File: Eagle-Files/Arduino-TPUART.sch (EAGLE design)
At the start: 18 parts, among them Q1 4,915MHz

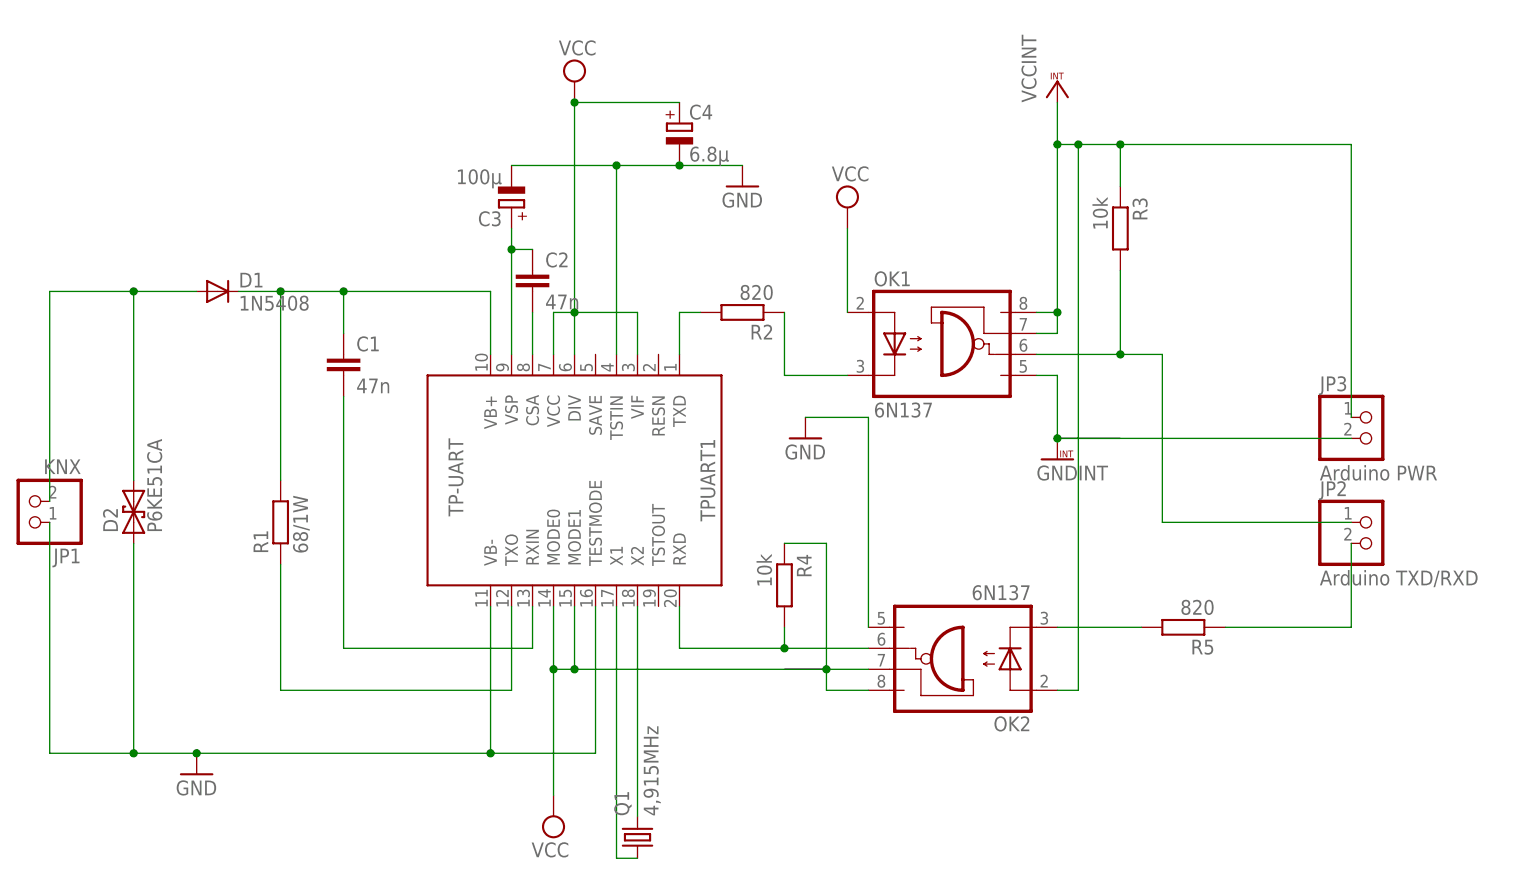
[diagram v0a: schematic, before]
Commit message: Update schematic with actually used parts and their correct packages.
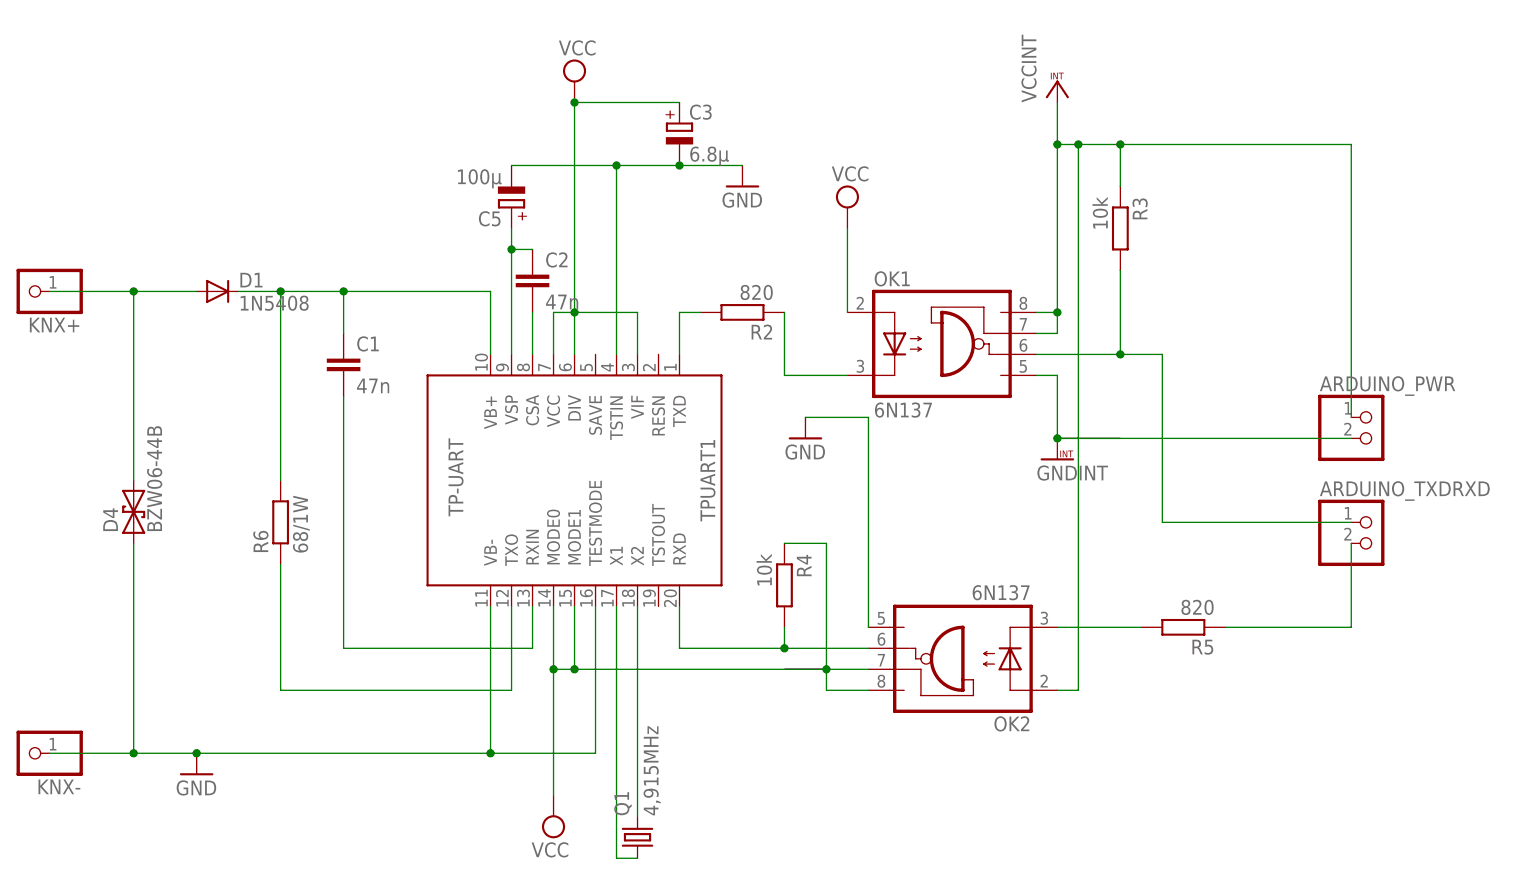
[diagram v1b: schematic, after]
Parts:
- removed C4: 6.8µ, rcl:CPOL-EUE5-4
- removed D2: P6KE51CA, diode:15KEXXC
- removed JP1: KNX, pinhead:PINHD-1X2
- removed R1: 68/1W, resistor:R-EU_0207/10
- added C5: 100µ, resistor:CPOL-EUE2.5-5
- added D4: BZW06-44B, diode:BZW04XXB
- added KNX+, KNX-: (no value), pinhead:PINHD-1X1
- added R6: 68/1W, resistor:R-EU_0414/15
- ARDUINO_PWR: value Arduino PWR -> (none)
- ARDUINO_TXDRXD: value Arduino TXD/RXD -> (none)
- C3: value 100µ -> 6.8µ; device rcl:CPOL-EUE5-4 -> resistor:CPOL-EUE2-5
- R2, R3, R4, R5: device resistor:R-EU_0207/10 -> resistor:R-EU_0411/12
- renumbered JP2 to ARDUINO_TXDRXD, JP3 to ARDUINO_PWR
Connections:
- net N$11 renamed ARDUINO_RXD
- net N$13 renamed ARDUINO_TXD
- removed net N$2: D1.A, D2.2, JP1.2
- new net KNX+: D1.A, D4.2, KNX+.1
- net GND: now also C5.-, D4.1, KNX-.1; no longer C4.-, D2.1, JP1.1
- net N$1: now also R6.2; no longer R1.2
- net N$3: now also R6.1; no longer R1.1
- net N$6: now also C5.+; no longer C3.+
- net VCC: now also C3.+; no longer C4.+
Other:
- moved on the sheet: C3

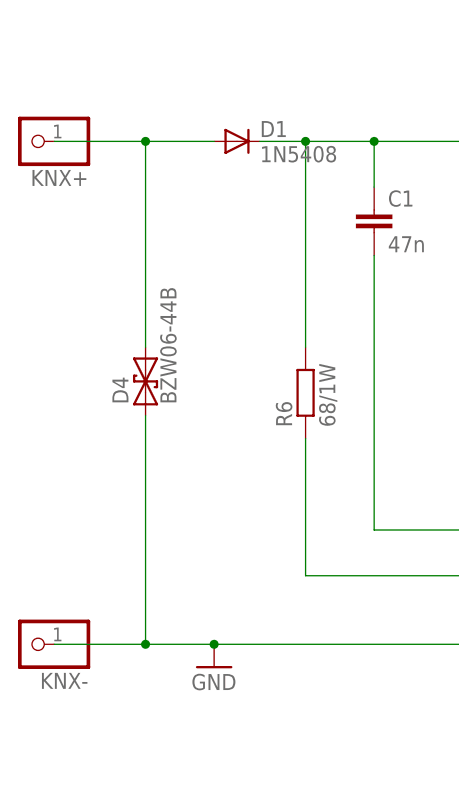
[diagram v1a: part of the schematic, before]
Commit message: Add board layout for putting the KNX adapter on a breadboard.
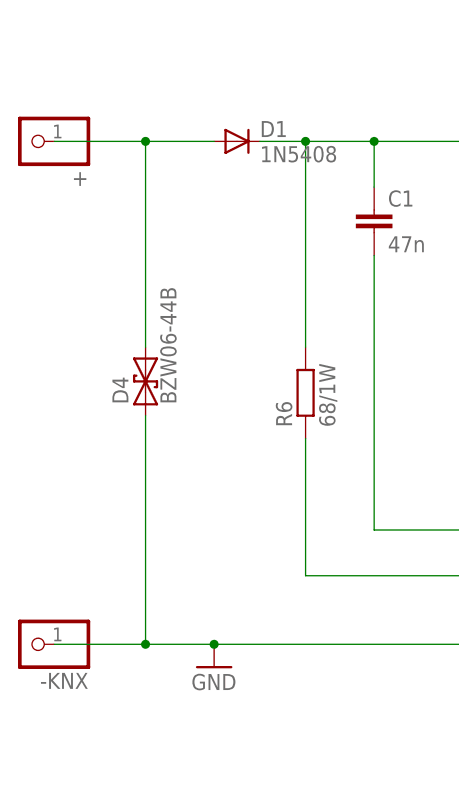
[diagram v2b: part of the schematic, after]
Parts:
- renumbered KNX+ to +, KNX- to -KNX
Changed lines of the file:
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@@
 <part name="C3" library="resistor" deviceset="CPOL-EU" device="E2-5" value="6.8µ"/>
 <part name="R6" library="resistor" deviceset="R-EU_" device="0414/15" value="68/1W"/>
-<part name="KNX+" library="pinhead" deviceset="PINHD-1X1" device=""/>
-<part name="KNX-" library="pinhead" deviceset="PINHD-1X1" device=""/>
+<part name="+" library="pinhead" deviceset="PINHD-1X1" device=""/>
+<part name="-KNX" library="pinhead" deviceset="PINHD-1X1" device=""/>
 </parts>
 <sheets>
@@
 <instance part="C3" gate="G$1" x="40.64" y="45.72"/>
 <instance part="R6" gate="G$1" x="-7.62" y="-2.54" rot="R90"/>
-<instance part="KNX+" gate="G$1" x="-38.1" y="25.4" rot="R180"/>
-<instance part="KNX-" gate="G$1" x="-38.1" y="-30.48" rot="R180"/>
+<instance part="+" gate="G$1" x="-38.1" y="25.4" rot="R180"/>
+<instance part="-KNX" gate="G$1" x="-38.1" y="-30.48" rot="R180"/>
 </instances>
 <busses>
@@
 <wire x1="-25.4" y1="25.4" x2="-25.4" y2="2.54" width="0.1524" layer="91"/>
 <pinref part="D4" gate="1" pin="2"/>
-<pinref part="KNX+" gate="G$1" pin="1"/>
+<pinref part="+" gate="G$1" pin="1"/>
 </segment>
 </net>
@@
 <wire x1="30.48" y1="-30.48" x2="30.48" y2="-12.7" width="0.1524" layer="91"/>
 <pinref part="D4" gate="1" pin="1"/>
-<pinref part="KNX-" gate="G$1" pin="1"/>
+<pinref part="-KNX" gate="G$1" pin="1"/>
 </segment>
 <segment>
